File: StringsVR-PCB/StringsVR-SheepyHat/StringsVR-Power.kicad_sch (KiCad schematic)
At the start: 19 parts, among them J1 MPU6050, J2 Conn_02x20_Odd_Even, SW1 ON/OFF

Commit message: added footprints, new pcb
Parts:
- removed SW1: ON/OFF, Button_Switch_THT:SW_Slide_SPDT_Angled_CK_OS102011MA1Q, symbol Switch:SW_SPDT
- added SW2: SRB22A2BBBNN, SW_SRB22A2BBBNN_ZFE, symbol SW_SRB22A2BBBNN_ZFE:SRB22A2BBBNN
- J1: footprint Arduino:MPU6050 -> Strings_Custom_Symbols:MPU6050
- J2: footprint Arduino:Pin_Header_Straight_2x20_Pitch2.54mm -> Strings_Custom_Symbols:Pin_Header_Straight_2x20_Pitch2.54mm
- U1: footprint Arduino:Pro Micro -> Strings_Custom_Symbols:Pro Micro
- U2, U3: footprint Arduino:nRF24L01 -> Strings_Custom_Symbols:nRF24L01
- renumbered U1 to U4, U4 to U6, U2 to U7, U3 to U8
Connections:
- net at U5.2 (VIN), U5.3 (VIN): now also SW2.2
- net at U4.3 (OUT+): now also SW2.1
- no-connect marks 59 -> 58

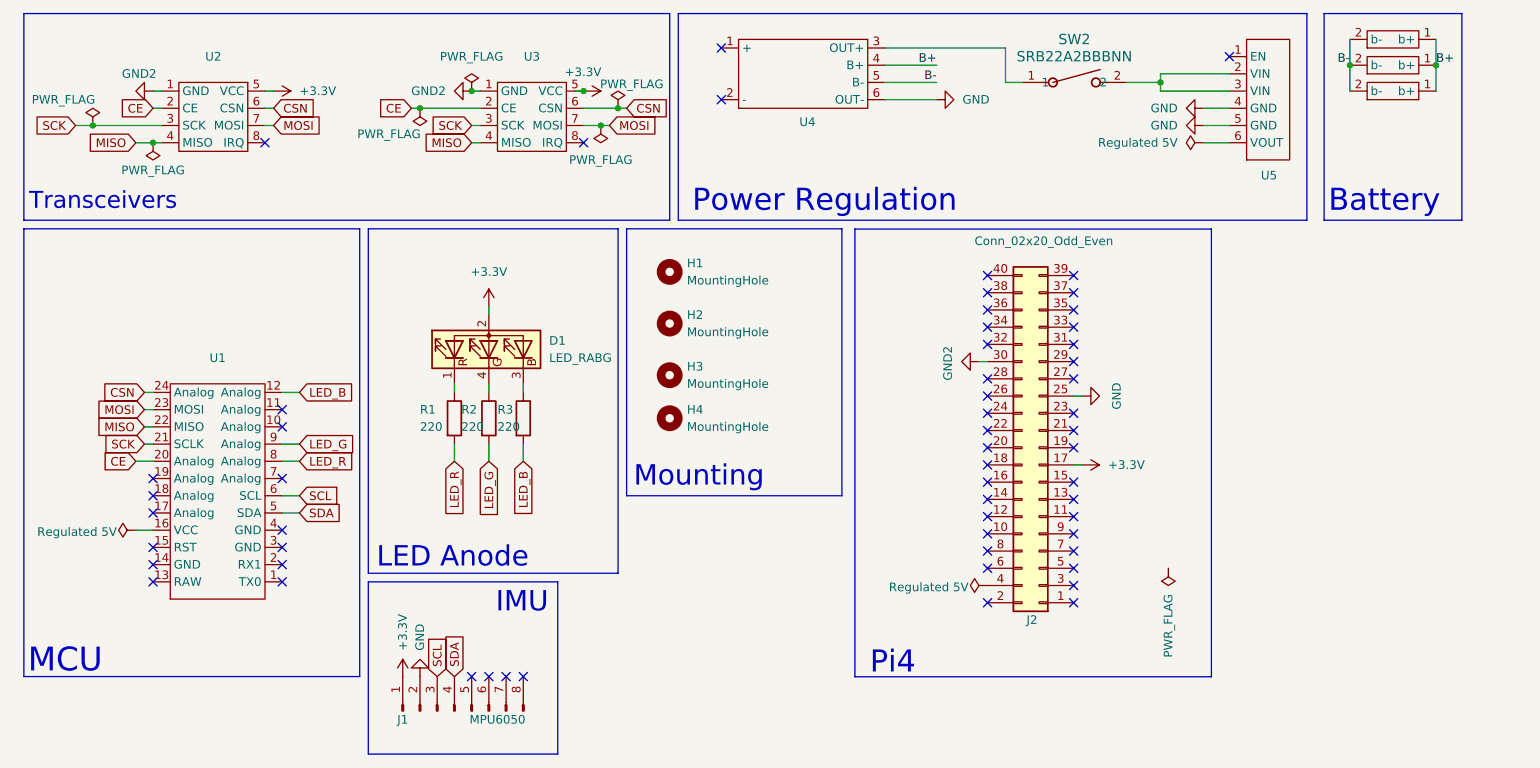
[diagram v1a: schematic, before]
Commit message: updated pcb design, new footprints, updated schem a lil
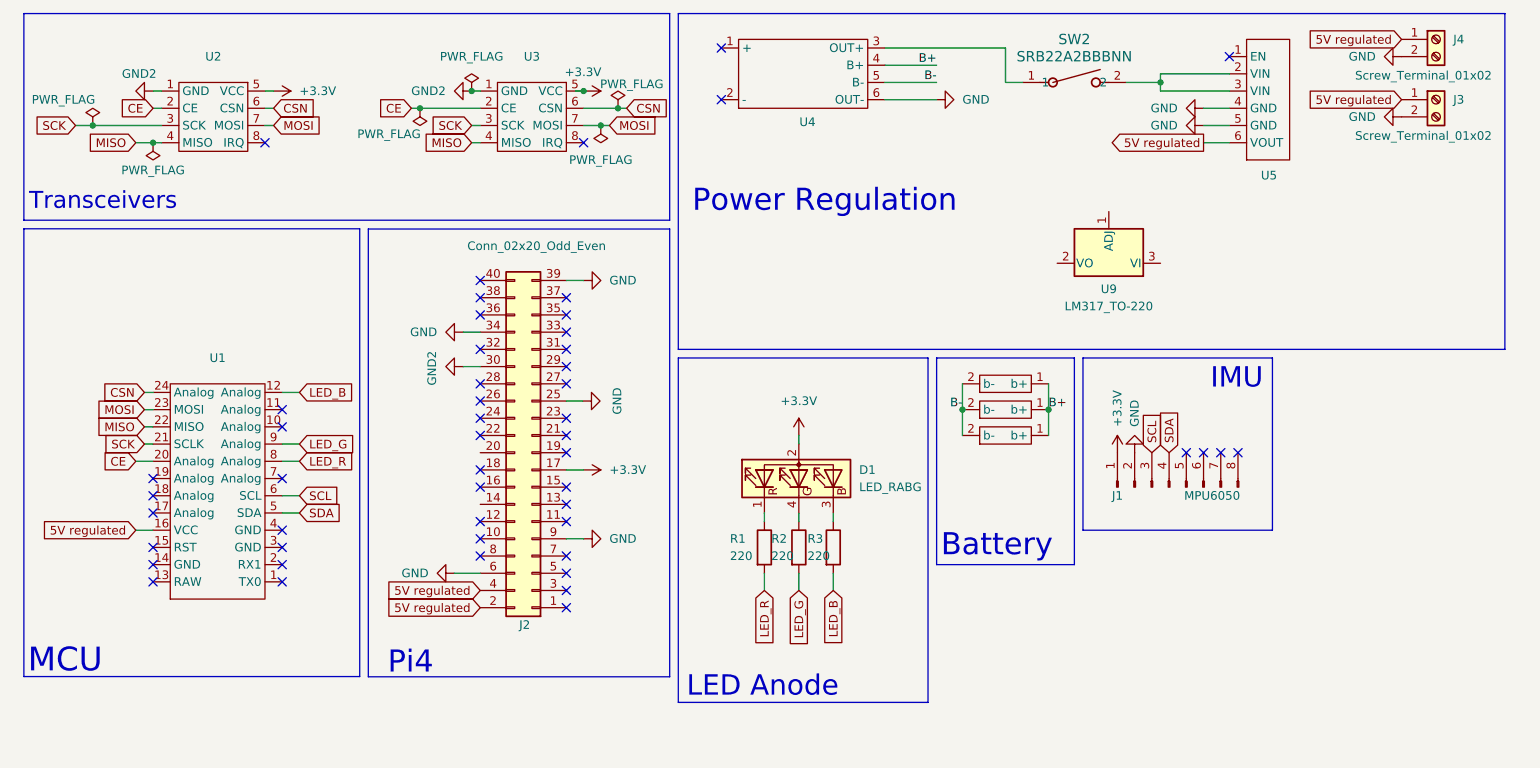
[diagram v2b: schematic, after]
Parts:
- removed H1, H2, H3, H4: MountingHole, MountingHole:MountingHole_2.7mm, symbol Mechanical:MountingHole
- added J3, J4: Screw_Terminal_01x02, Strings_Custom_Symbols:CUI_TB003-500-P02BE, symbol Connector:Screw_Terminal_01x02
- added U9: LM317_TO-220, Package_TO_SOT_THT:TO-220-3_Horizontal_TabDown, symbol Regulator_Linear:LM317_TO-220
- U6, U7, U8: footprint 18650:18650PCB -> Strings_Custom_Symbols:18650SMD
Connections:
- net GND: now also J2.34 (Pin_34), J2.39 (Pin_39), J2.6 (Pin_6), J2.9 (Pin_9), J3.2 (Pin_2), J4.2 (Pin_2)
- net 5V regulated: now reaches U5.6 (VOUT)
- net 5V regulated: now also J2.2 (Pin_2), J2.4 (Pin_4), U1.16 (VCC), J3.1 (Pin_1), J4.1 (Pin_1)
- no-connect marks 58 -> 51
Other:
- note removed: "Mounting"
- moved on the sheet: D1, J1, J2, R1, R2, R3
